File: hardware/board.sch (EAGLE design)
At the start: 83 parts, among them CON2 USB-FPGA-2THT, IC1 THS3062

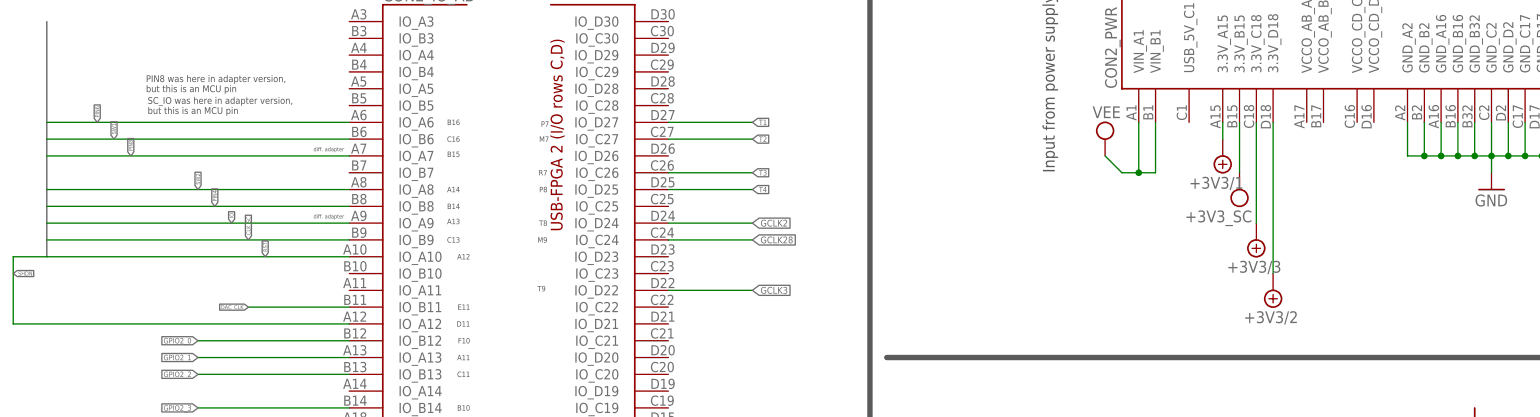
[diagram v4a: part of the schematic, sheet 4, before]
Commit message: Fully routed and freed some space for ADC in middle/right
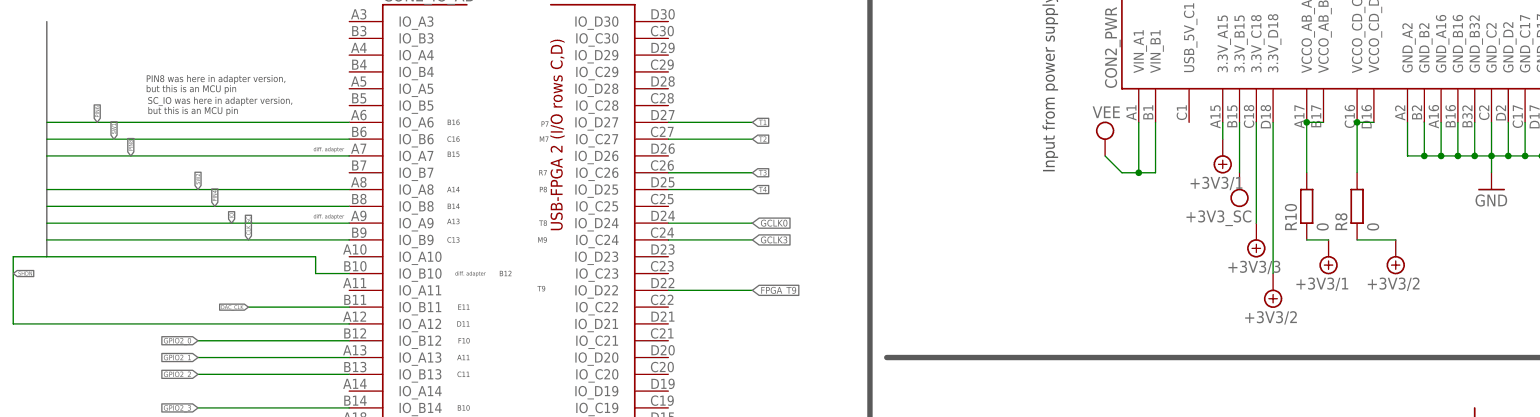
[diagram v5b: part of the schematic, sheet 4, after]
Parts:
- added R10, R8: 0, rcl:R-EU_R0805
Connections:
- net GCLK2 renamed GCLK0
- removed net GCLK28: CON2_IO_CD.IO_C24, JP7.2
- new net FPGA_T9: CON2_IO_CD.IO_D22, JP7.1
- new net N$1: CON2_PWR.VCCO_AB_A17, CON2_PWR.VCCO_AB_B17, R10.2
- new net N$2: CON2_PWR.VCCO_CD_C16, CON2_PWR.VCCO_CD_D16, R8.2
- net +5V/1: now also R10.1
- net +5V/2: now also R8.1
- net GCLK3: now also CON2_IO_CD.IO_C24, JP7.2; no longer CON2_IO_CD.IO_D22, JP7.1
- net RST: now also CON2_IO_AB.IO_B10; no longer CON2_IO_AB.IO_A10
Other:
- note added: "B12"
- note removed: "A12"
- note removed: "not GCLK"
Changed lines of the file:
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@@
 <part name="SUPPLY1" library="supply2" deviceset="+5V/1" device="" value="+3V3/1"/>
 <part name="SUPPLY3" library="supply2" deviceset="+5V/1" device="" value="+3V3/1"/>
+<part name="R10" library="rcl" deviceset="R-EU_" device="R0805" value="0"/>
+<part name="R8" library="rcl" deviceset="R-EU_" device="R0805" value="0"/>
+<part name="SUPPLY4" library="supply2" deviceset="+5V/1" device="" value="+3V3/1"/>
+<part name="SUPPLY17" library="supply2" deviceset="+5V/2" device="" value="+3V3/2"/>
 </parts>
 <sheets>
@@
 </segment>
 </net>
-<net name="GCLK3" class="0">
+<net name="FPGA_T9" class="0">
 <segment>
 <pinref part="JP7" gate="A" pin="1"/>
@@
 </segment>
 </net>
-<net name="GCLK28" class="0">
+<net name="GCLK3" class="0">
 <segment>
 <pinref part="JP7" gate="A" pin="2"/>
@@
 </segment>
 </net>
-<net name="GCLK2" class="0">
+<net name="GCLK0" class="0">
 <segment>
 <pinref part="JP7" gate="A" pin="3"/>
@@
 <text x="77.724" y="129.794" size="0.8128" layer="97" align="center-right">A13</text>
 <text x="77.724" y="127" size="0.8128" layer="97" align="center-right">C13</text>
-<text x="79.248" y="124.46" size="0.8128" layer="97" align="center-right">A12</text>
-<text x="55.626" y="123.444" size="0.8128" layer="150" align="center-right">check, VREF!</text>
+<text x="85.598" y="121.92" size="0.8128" layer="97" align="center-right">B12</text>
 <text x="79.248" y="116.84" size="0.8128" layer="97" align="center-right">E11</text>
 <text x="79.248" y="114.3" size="0.8128" layer="97" align="center-right">D11</text>
@@
 <text x="90.932" y="127" size="0.8128" layer="97" align="center-right">M9</text>
 <text x="90.932" y="129.54" size="0.8128" layer="97" align="center-right">T8</text>
-<text x="119.126" y="120.396" size="0.8128" layer="150" align="center-right">not GCLK</text>
 <text x="90.932" y="134.62" size="0.8128" layer="97" align="center-right">P8</text>
 <text x="90.932" y="137.16" size="0.8128" layer="97" align="center-right">R7</text>
@@
 <wire x1="139.7" y1="172.72" x2="139.7" y2="10.16" width="0.8128" layer="97"/>
 <wire x1="142.24" y1="109.22" x2="254" y2="109.22" width="0.8128" layer="97"/>
+<text x="76.962" y="121.92" size="0.6096" layer="97" rot="R180" align="center-right">diff. adapter</text>
 </plain>
 <instances>
@@
 <instance part="SUPPLY42" gate="G$1" x="200.66" y="119.38" rot="R180"/>
 <instance part="SUPPLY43" gate="G$1" x="198.12" y="127" rot="R180"/>
+<instance part="R10" gate="G$1" x="205.74" y="132.08" rot="R90"/>
+<instance part="R8" gate="G$1" x="213.36" y="132.08" rot="R90"/>
+<instance part="SUPPLY4" gate="G$1" x="209.042" y="124.46" rot="R180"/>
+<instance part="SUPPLY17" gate="G$1" x="219.202" y="124.46" rot="R180"/>
 </instances>
 <busses>
@@
 <wire x1="193.04" y1="142.24" x2="193.04" y2="144.78" width="0.1524" layer="91"/>
 </segment>
+<segment>
+<pinref part="R10" gate="G$1" pin="1"/>
+<pinref part="SUPPLY4" gate="G$1" pin="+5V/1"/>
+<wire x1="209.042" y1="127" x2="205.74" y2="127" width="0.1524" layer="91"/>
+</segment>
 </net>
 <net name="VPP" class="0">
@@
 <wire x1="200.66" y1="121.92" x2="200.66" y2="144.78" width="0.1524" layer="91"/>
 </segment>
+<segment>
+<pinref part="R8" gate="G$1" pin="1"/>
+<wire x1="213.36" y1="127" x2="219.202" y2="127" width="0.1524" layer="91"/>
+<pinref part="SUPPLY17" gate="G$1" pin="+5V/2"/>
+</segment>
 </net>
 <net name="LED1_PIN" class="0">
@@
 </segment>
 </net>
-<net name="GCLK3" class="0">
+<net name="FPGA_T9" class="0">
 <segment>
 <wire x1="109.22" y1="119.38" x2="121.92" y2="119.38" width="0.1524" layer="91"/>
@@
 </segment>
 </net>
-<net name="GCLK28" class="0">
+<net name="GCLK3" class="0">
 <segment>
 <wire x1="109.22" y1="127" x2="121.92" y2="127" width="0.1524" layer="91"/>
@@
 </segment>
 </net>
-<net name="GCLK2" class="0">
+<net name="GCLK0" class="0">
 <segment>
 <wire x1="109.22" y1="129.54" x2="121.92" y2="129.54" width="0.1524" layer="91"/>
@@
 </segment>
 </net>
-<net name="RST" class="0">
-<segment>
-<pinref part="CON2" gate="_IO_AB" pin="IO_A10"/>
-<wire x1="60.96" y1="124.46" x2="15.24" y2="124.46" width="0.1524" layer="91"/>
-<label x="48.26" y="124.46" size="0.6096" layer="95" rot="R90" xref="yes"/>
-</segment>
-</net>
 <net name="DB5" class="0">
 <segment>
@@
 </segment>
 </net>
+<net name="N$1" class="0">
+<segment>
+<pinref part="CON2" gate="_PWR" pin="VCCO_AB_A17"/>
+<pinref part="CON2" gate="_PWR" pin="VCCO_AB_B17"/>
+<wire x1="205.74" y1="144.78" x2="208.28" y2="144.78" width="0.1524" layer="91"/>
+<wire x1="205.74" y1="144.78" x2="205.74" y2="137.16" width="0.1524" layer="91"/>
+<junction x="205.74" y="144.78"/>
+<pinref part="R10" gate="G$1" pin="2"/>
+</segment>
+</net>
+<net name="N$2" class="0">
+<segment>
+<pinref part="CON2" gate="_PWR" pin="VCCO_CD_C16"/>
+<pinref part="CON2" gate="_PWR" pin="VCCO_CD_D16"/>
+<wire x1="213.36" y1="144.78" x2="215.9" y2="144.78" width="0.1524" layer="91"/>
+<wire x1="213.36" y1="144.78" x2="213.36" y2="137.16" width="0.1524" layer="91"/>
+<junction x="213.36" y="144.78"/>
+<pinref part="R8" gate="G$1" pin="2"/>
+</segment>
+</net>
+<net name="RST" class="0">
+<segment>
+<wire x1="15.24" y1="124.46" x2="55.88" y2="124.46" width="0.1524" layer="91"/>
+<pinref part="CON2" gate="_IO_AB" pin="IO_B10"/>
+<wire x1="55.88" y1="124.46" x2="55.88" y2="121.92" width="0.1524" layer="91"/>
+<wire x1="55.88" y1="121.92" x2="60.96" y2="121.92" width="0.1524" layer="91"/>
+</segment>
+</net>

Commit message: Added ADC schematics etc, missing: FPGA pins and routing
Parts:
- added C11, C12: 1µ, rcl:C-EUC1206
- added C13: 100n, rcl:C-EUC0805
- added CD1, CD3, CD6, CD8, CD_AMP, C_DEC_IN, C_DEC_OUT, C_REF1, C_REF3, C_REF4, C_REF6: 100n, rcl:C-EUC0603
- added CD2, CD4, CD5: 10n, rcl:C-EUC0603
- added CD9: 4.7µ, rcl:C-EUC1206
- added C_F+, C_F-: opt., rcl:C-EUC0603
- added C_REF2, C_REF5: 10µ, rcl:C-EUC1206
- added IC2: AD80XX, ad80xx:AD80XX
- added L1: 120n, footprint?, SparkFun:INDUCTOR0805
- added R11, R12: 10k, rcl:R-EU_R0805
- added R9: optional, rcl:R-EU_R0805
- added R_F+, R_F-, R_T_IN: 49, rcl:R-EU_R0603
- added R_FB+, R_FB-: 1k, rcl:R-EU_R0603
- added R_FI, R_GI: 20k, rcl:R-EU_R0603
- added R_GND: 0, rcl:R-EU_R0805
- added R_IN+: 499, rcl:R-EU_R0603
- added R_IN-: 523, rcl:R-EU_R0603
- added SJ1, SJ2: 0R, jumper:SJ
- added TP_GNDA1, TP_IN: TPPAD1-13, testpad:TPPAD1-13
- added U$18: TS5204, ts5204:TS5204
- added U$7: AD8138, ad8138:AD8138
- added U1: AD9215BRUZ, ad9215bruz:AD9215BRUZ
- added X1: BU-SMA-V, con-coax-sma-adapted:BU-SMA-V
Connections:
- new net ADC_CLK: R9.2, SJ2.1, U1.CLK
- new net ADC_CLK_FB: SJ2.2
- new net ADC_D0: U1.D0
- new net ADC_D1: U1.D1
- new net ADC_D2: U1.D2
- new net ADC_D3: U1.D3
- new net ADC_D4: U1.D4
- new net ADC_D5: U1.D5
- new net ADC_D6: U1.D6
- new net ADC_D7: U1.D7
- new net ADC_D8: U1.D8
- new net ADC_D9: U1.D9
- new net ADC_IN+: C_F+.2, R_F+.1, U1.VIN+
- new net ADC_IN-: C_F-.1, R_F-.1, U1.VIN-
- new net ADC_OR: U1.OR
- new net ADC_V_REF: C_REF5.2, C_REF6.2, SJ1.1, U1.VREF
- new net AMP_IN+: R_FB-.2, R_IN+.1, U$7.IN+
- new net AMP_IN-: R_FB+.1, R_IN-.1, U$7.IN-
- new net AMP_OUT+: R_F+.2, R_FB+.2, U$7.OUT+
- new net AMP_OUT-: R_F-.2, R_FB-.1, U$7.OUT-
- new net GND2: C11.2, C12.2, C13.2, CD1.2, CD2.2, CD3.2, CD4.2, CD8.2, CD9.1, CD_AMP.2, C_F+.1, C_F-.2, C_REF3.1, C_REF4.1, C_REF5.1, C_REF6.1, R12.1, R_GND.1, R_IN-.2, R_T_IN.2, TP_GNDA1.TP, U$18.GND, U$7.V-, U1.AGND@0, U1.AGND@1, U1.MODE, U1.PDWN, X1G$1.GND, X1G2.GND, X1G3.GND, X1G4.GND
- new net IN_ADC_AMP: C_DEC_OUT.2, R_IN+.2, R_T_IN.1
- new net N$21: C_DEC_OUT.1, IC2AD80XXOP1.OUT, R_FI.2
- new net N$25: IC2AD80XXOP1.IN-, R_FI.1, R_GI.2
- new net N$3: C11.1, L1.1, U$18.IN
- new net N$4: SJ1.2, U1.SENSE
- new net N$5: C_REF1.2, C_REF2.2, C_REF3.2, U1.REFT
- new net N$6: C_REF1.1, C_REF2.1, C_REF4.2, U1.REFB
- new net N$8: C_DEC_IN.1, TP_IN.TP, X1G$1.1
- new net N$9: C_DEC_IN.2, IC2AD80XXOP1.IN+
- new net OP-: IC2SUPPLY.VCC-
- new net VCC_ADC: CD5.1, CD6.1, U1.DRVDD
- new net V_15: IC2AD80XXOP2.IN-, IC2AD80XXOP2.OUT, R_GI.1, U$7.V_OCM
- new net V_15_UNBUF: C13.1, IC2AD80XXOP2.IN+, R11.1, R12.2
- new net V_ANALOG: C12.1, CD1.1, CD2.1, CD3.1, CD4.1, CD8.1, CD9.2, CD_AMP.1, IC2SUPPLY.VCC+, R11.2, U$18.OUT, U$7.V+, U1.AVDD@0, U1.AVDD@1
- net +5V/3: now also L1.2
- net GND: now also CD5.2, CD6.2, R9.1, R_GND.2, U1.DRGND
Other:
- note added: "+"
- note added: "2.4k"
- note added: "CHANGE: XC6206P302MR 3V LDO, 90 deg rotated or other 3V"
- note added: "Check if 3V ok?"
- note added: "Clock feedback?"
- note added: "Feedback for gain = 2"
- note added: "Generate 1.5V from 3V"

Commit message: Added ADC pins (unrouted) Moved GCLK pins
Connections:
- removed net FPGA_T9: CON2_IO_CD.IO_D22, JP7.1
- removed net GCLK0: CON2_IO_CD.IO_D24, JP7.3
- removed net GCLK3: CON2_IO_CD.IO_C24, JP7.2
- new net DAC_SLEEP: AD9708.SLEEP
- new net FPGA_R9: CON2_IO_CD.IO_D23, JP7.1
- new net GCLK2: CON2_IO_CD.IO_C25, JP7.2
- new net GCLK28: CON2_IO_CD.IO_D26, JP7.3
- net ADC_CLK: now also CON2_IO_CD.IO_D24
- net ADC_CLK_FB: now also CON2_IO_CD.IO_C24
- net ADC_D0: now also CON2_IO_CD.IO_C15
- net ADC_D1: now also CON2_IO_CD.IO_D15
- net ADC_D2: now also CON2_IO_CD.IO_C19
- net ADC_D3: now also CON2_IO_CD.IO_D19
- net ADC_D4: now also CON2_IO_CD.IO_C20
- net ADC_D5: now also CON2_IO_CD.IO_D20
- net ADC_D6: now also CON2_IO_CD.IO_C21
- net ADC_D7: now also CON2_IO_CD.IO_D21
- net ADC_D8: now also CON2_IO_CD.IO_C22
- net ADC_D9: now also CON2_IO_CD.IO_D22
- net ADC_OR: now also CON2_IO_CD.IO_C23
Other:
- note added: "Clock feedback"
- note added: "Input span = 1V"
- note added: "Input span = 500mV (for gain = 2, Vref = 0.5V)"
- note added: "R9"
- note added: "Vref = 0.5V"
- note removed: "ADC here?"
- note removed: "Clock feedback?"
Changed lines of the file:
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@@
 <wire x1="88.9" y1="38.1" x2="111.76" y2="15.24" width="0.1524" layer="97"/>
 <wire x1="111.76" y1="15.24" x2="111.76" y2="10.16" width="0.1524" layer="97"/>
-<text x="76.2" y="35.56" size="1.016" layer="150" align="bottom-right">Connect so that FPGA has to
+<text x="73.66" y="33.02" size="1.016" layer="150" align="bottom-right">Connect so that FPGA has to
 start DAC?</text>
 </plain>
@@
 </segment>
 </net>
+<net name="DAC_SLEEP" class="0">
+<segment>
+<pinref part="AD9708" gate="AD9708" pin="SLEEP"/>
+<wire x1="76.2" y1="38.1" x2="71.12" y2="38.1" width="0.1524" layer="91"/>
+<label x="71.12" y="38.1" size="1.4224" layer="95" rot="R180" xref="yes"/>
+</segment>
+</net>
 </nets>
 </sheet>
@@
 <text x="144.272" y="166.624" size="1.778" layer="150">CHANGE: XC6206P302MR 3V LDO, 90 deg rotated
 or other 3V</text>
-<text x="172.72" y="124.46" size="1.778" layer="150">Clock feedback?</text>
+<text x="172.72" y="124.46" size="1.778" layer="97">Clock feedback</text>
 <wire x1="139.7" y1="101.6" x2="254" y2="101.6" width="0.6096" layer="97"/>
 <text x="36.576" y="43.434" size="2.54" layer="91">+</text>
@@
 <text x="182.88" y="45.72" size="1.9304" layer="97">Generate 1.5V
 from 3V</text>
+<text x="49.53" y="53.594" size="1.4224" layer="97" rot="R90">Vref = 0.5V</text>
+<text x="76.454" y="44.45" size="1.4224" layer="97" rot="R180">Input span = 1V</text>
+<text x="16.51" y="142.748" size="1.4224" layer="97">Input span = 500mV
+(for gain = 2, Vref = 0.5V)</text>
+<text x="206.756" y="93.726" size="1.4224" layer="97" rot="R180">Feedback for gain = 2</text>
 </plain>
 <instances>
@@
 </segment>
 </net>
-<net name="FPGA_T9" class="0">
+<net name="FPGA_R9" class="0">
 <segment>
 <pinref part="JP7" gate="A" pin="1"/>
@@
 </segment>
 </net>
-<net name="GCLK3" class="0">
+<net name="GCLK2" class="0">
 <segment>
 <pinref part="JP7" gate="A" pin="2"/>
@@
 </segment>
 </net>
-<net name="GCLK0" class="0">
+<net name="GCLK28" class="0">
 <segment>
 <pinref part="JP7" gate="A" pin="3"/>
@@
 <text x="91.186" y="142.24" size="0.8128" layer="97" align="center-right">M7</text>
 <text x="91.186" y="144.526" size="0.8128" layer="97" align="center-right">P7</text>
-<text x="114.3" y="111.76" size="1.6764" layer="150" rot="R90" align="center-right">ADC here?</text>
 <wire x1="139.7" y1="172.72" x2="139.7" y2="10.16" width="0.8128" layer="97"/>
 <wire x1="142.24" y1="109.22" x2="254" y2="109.22" width="0.8128" layer="97"/>
 <text x="76.962" y="121.92" size="0.6096" layer="97" rot="R180" align="center-right">diff. adapter</text>
+<text x="90.932" y="124.714" size="0.8128" layer="97" align="center-right">R9</text>
 </plain>
 <instances>
@@
 </segment>
 </net>
-<net name="FPGA_T9" class="0">
-<segment>
-<wire x1="109.22" y1="119.38" x2="121.92" y2="119.38" width="0.1524" layer="91"/>
-<label x="121.92" y="119.38" size="1.016" layer="95" xref="yes"/>
-<pinref part="CON2" gate="_IO_CD" pin="IO_D22"/>
-</segment>
-</net>
-<net name="GCLK3" class="0">
-<segment>
-<wire x1="109.22" y1="127" x2="121.92" y2="127" width="0.1524" layer="91"/>
-<label x="121.92" y="127" size="1.016" layer="95" xref="yes"/>
-<pinref part="CON2" gate="_IO_CD" pin="IO_C24"/>
-</segment>
-</net>
-<net name="GCLK0" class="0">
-<segment>
-<wire x1="109.22" y1="129.54" x2="121.92" y2="129.54" width="0.1524" layer="91"/>
-<label x="121.92" y="129.54" size="1.016" layer="95" xref="yes"/>
-<pinref part="CON2" gate="_IO_CD" pin="IO_D24"/>
+<net name="GCLK2" class="0">
+<segment>
+<pinref part="CON2" gate="_IO_CD" pin="IO_C25"/>
+<wire x1="109.22" y1="132.08" x2="121.92" y2="132.08" width="0.1524" layer="91"/>
+<label x="121.92" y="132.08" size="0.8128" layer="95" xref="yes"/>
+</segment>
+</net>
+<net name="GCLK28" class="0">
+<segment>
+<pinref part="CON2" gate="_IO_CD" pin="IO_D26"/>
+<wire x1="109.22" y1="139.7" x2="121.92" y2="139.7" width="0.1524" layer="91"/>
+<label x="121.92" y="139.7" size="0.8128" layer="95" xref="yes"/>
 </segment>
 </net>
@@
 </segment>
 </net>
+<net name="ADC_D2" class="0">
+<segment>
+<pinref part="CON2" gate="_IO_CD" pin="IO_C19"/>
+<wire x1="109.22" y1="101.6" x2="121.92" y2="101.6" width="0.1524" layer="91"/>
+<label x="121.92" y="101.6" size="0.8128" layer="95" xref="yes"/>
+</segment>
+</net>
+<net name="ADC_D0" class="0">
+<segment>
+<pinref part="CON2" gate="_IO_CD" pin="IO_C15"/>
+<wire x1="109.22" y1="96.52" x2="121.92" y2="96.52" width="0.1524" layer="91"/>
+<label x="121.92" y="96.52" size="0.8128" layer="95" xref="yes"/>
+</segment>
+</net>
+<net name="ADC_D1" class="0">
+<segment>
+<pinref part="CON2" gate="_IO_CD" pin="IO_D15"/>
+<wire x1="109.22" y1="99.06" x2="121.92" y2="99.06" width="0.1524" layer="91"/>
+<label x="121.92" y="99.06" size="0.8128" layer="95" xref="yes"/>
+</segment>
+</net>
+<net name="ADC_D3" class="0">
+<segment>
+<pinref part="CON2" gate="_IO_CD" pin="IO_D19"/>
+<wire x1="109.22" y1="104.14" x2="121.92" y2="104.14" width="0.1524" layer="91"/>
+<label x="121.92" y="104.14" size="0.8128" layer="95" xref="yes"/>
+</segment>
+</net>
+<net name="ADC_D4" class="0">
+<segment>
+<pinref part="CON2" gate="_IO_CD" pin="IO_C20"/>
+<wire x1="109.22" y1="106.68" x2="121.92" y2="106.68" width="0.1524" layer="91"/>
+<label x="121.92" y="106.68" size="0.8128" layer="95" xref="yes"/>
+</segment>
+</net>
+<net name="ADC_D5" class="0">
+<segment>
+<pinref part="CON2" gate="_IO_CD" pin="IO_D20"/>
+<wire x1="109.22" y1="109.22" x2="121.92" y2="109.22" width="0.1524" layer="91"/>
+<label x="121.92" y="109.22" size="0.8128" layer="95" xref="yes"/>
+</segment>
+</net>
+<net name="ADC_D6" class="0">
+<segment>
+<pinref part="CON2" gate="_IO_CD" pin="IO_C21"/>
+<wire x1="109.22" y1="111.76" x2="121.92" y2="111.76" width="0.1524" layer="91"/>
+<label x="121.92" y="111.76" size="0.8128" layer="95" xref="yes"/>
+</segment>
+</net>
+<net name="ADC_D7" class="0">
+<segment>
+<pinref part="CON2" gate="_IO_CD" pin="IO_D21"/>
+<wire x1="109.22" y1="114.3" x2="121.92" y2="114.3" width="0.1524" layer="91"/>
+<label x="121.92" y="114.3" size="0.8128" layer="95" xref="yes"/>
+</segment>
+</net>
+<net name="ADC_D8" class="0">
+<segment>
+<pinref part="CON2" gate="_IO_CD" pin="IO_C22"/>
+<wire x1="109.22" y1="116.84" x2="121.92" y2="116.84" width="0.1524" layer="91"/>
+<label x="121.92" y="116.84" size="0.8128" layer="95" xref="yes"/>
+</segment>
+</net>
+<net name="ADC_CLK_FB" class="0">
+<segment>
+<pinref part="CON2" gate="_IO_CD" pin="IO_C24"/>
+<wire x1="109.22" y1="127" x2="121.92" y2="127" width="0.1524" layer="91"/>
+<label x="121.92" y="127" size="0.8128" layer="95" xref="yes"/>
+</segment>
+</net>
+<net name="ADC_CLK" class="0">
+<segment>
+<pinref part="CON2" gate="_IO_CD" pin="IO_D24"/>
+<wire x1="109.22" y1="129.54" x2="121.92" y2="129.54" width="0.1524" layer="91"/>
+<label x="121.92" y="129.54" size="0.8128" layer="95" xref="yes"/>
+</segment>
+</net>
+<net name="FPGA_R9" class="0">
+<segment>
+<pinref part="CON2" gate="_IO_CD" pin="IO_D23"/>
+<wire x1="109.22" y1="124.46" x2="121.92" y2="124.46" width="0.1524" layer="91"/>
+<label x="121.92" y="124.46" size="0.8128" layer="95" xref="yes"/>
+</segment>
+</net>
+<net name="ADC_D9" class="0">
+<segment>
+<pinref part="CON2" gate="_IO_CD" pin="IO_D22"/>
+<wire x1="109.22" y1="119.38" x2="121.92" y2="119.38" width="0.1524" layer="91"/>
+<label x="121.92" y="119.38" size="0.8128" layer="95" xref="yes"/>
+</segment>
+</net>
+<net name="ADC_OR" class="0">
+<segment>
+<pinref part="CON2" gate="_IO_CD" pin="IO_C23"/>
+<wire x1="109.22" y1="121.92" x2="121.92" y2="121.92" width="0.1524" layer="91"/>
+<label x="121.92" y="121.92" size="0.8128" layer="95" xref="yes"/>
+</segment>
+</net>
